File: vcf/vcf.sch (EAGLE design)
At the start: 102 parts, among them IC1 OPA4130U, IC2 OPA4130U, IC3 OPA4130U, IC4 OPA4130U, IC5 OPA4130U, Q1 BC847ASMD, Q2 BC847ASMD, Q3 BC847ASMD, Q4 BC847ASMD, Q5 BC847ASMD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

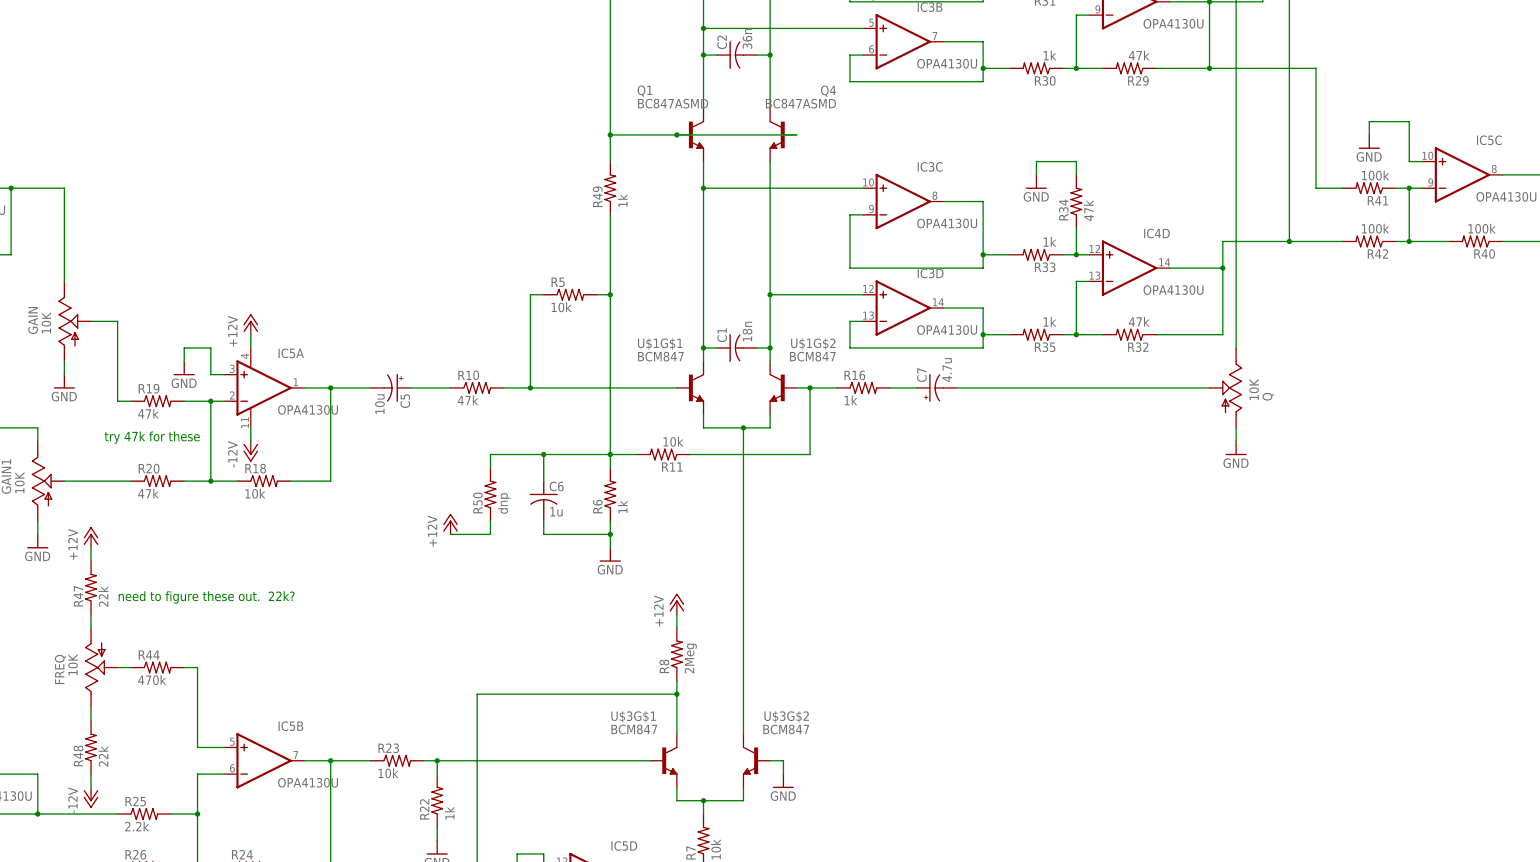
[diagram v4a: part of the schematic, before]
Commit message: fixed bugs in vca.  did more changing of vcf components.  need to route a trace in vcf
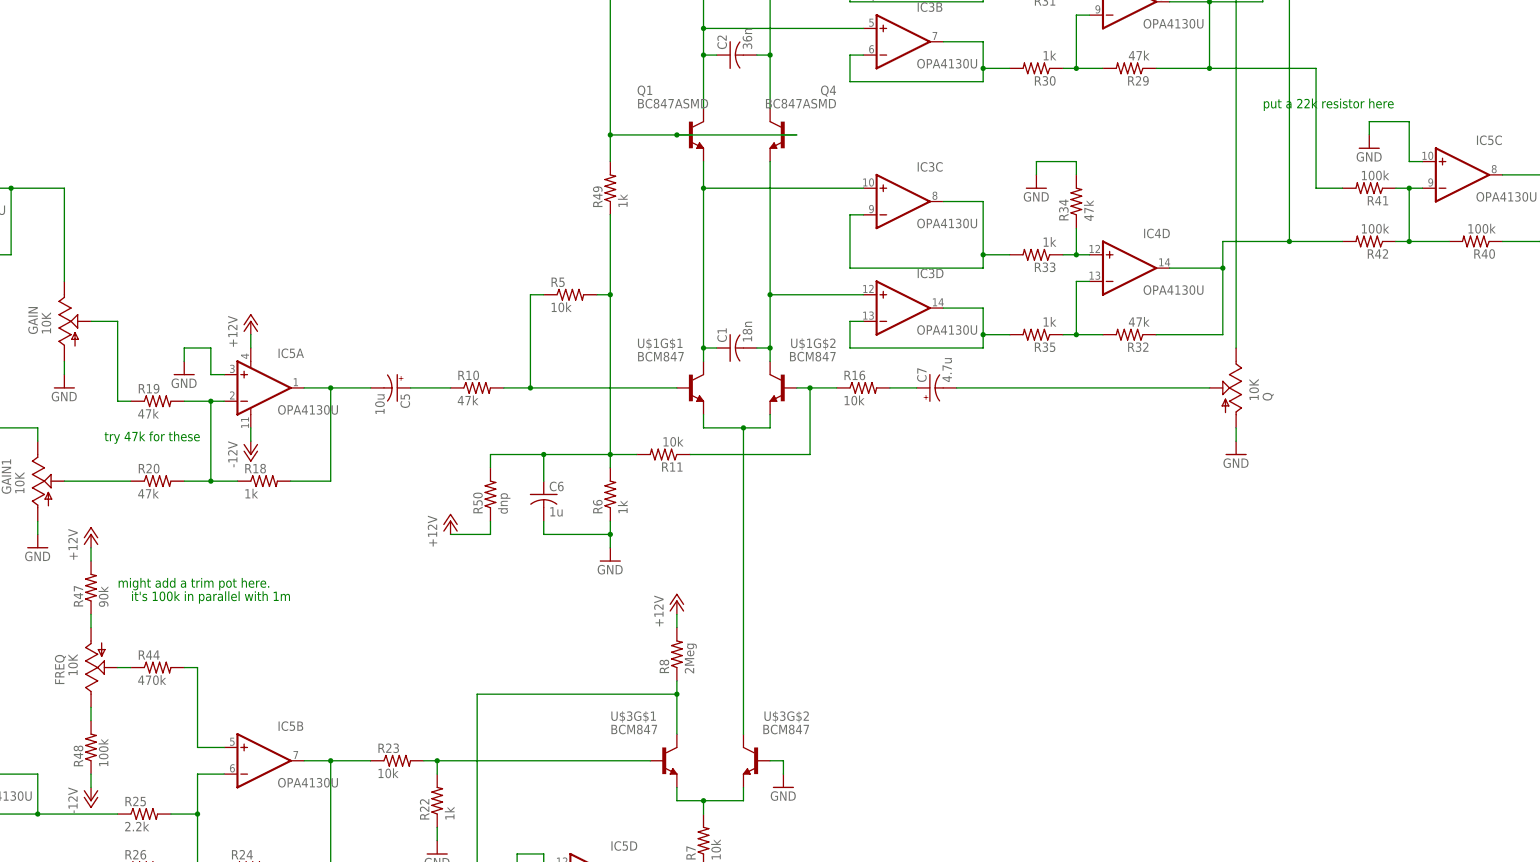
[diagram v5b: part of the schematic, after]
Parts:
- R16: value 1k -> 10k
- R18: value 10k -> 1k
- R47: value 22k -> 90k
- R48: value 22k -> 100k
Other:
- note added: "it's 100k in parallel with 1m"
- note added: "might add a trim pot here."
- note added: "put a 22k resistor here"
- note removed: "need to figure these out. 22k?"
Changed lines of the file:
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@@
 <part name="R15" library="dan" deviceset="R-US_" device="R0603" value="47k"/>
 <part name="GND5" library="dan" deviceset="GND" device=""/>
-<part name="R16" library="dan" deviceset="R-US_" device="R0603" value="1k"/>
+<part name="R16" library="dan" deviceset="R-US_" device="R0603" value="10k"/>
 <part name="Q" library="dan" deviceset="US-EVU" device="F2J" value="10K"/>
-<part name="R18" library="dan" deviceset="R-US_" device="R0603" value="10k"/>
+<part name="R18" library="dan" deviceset="R-US_" device="R0603" value="1k"/>
 <part name="R19" library="dan" deviceset="R-US_" device="R0603" value="47k"/>
 <part name="R20" library="dan" deviceset="R-US_" device="R0603" value="47k"/>
@@
 <part name="R45" library="dan" deviceset="R-US_" device="R0603" value="1k"/>
 <part name="R46" library="dan" deviceset="R-US_" device="R0603" value="1k"/>
-<part name="R47" library="dan" deviceset="R-US_" device="R0603" value="22k"/>
-<part name="R48" library="dan" deviceset="R-US_" device="R0603" value="22k"/>
+<part name="R47" library="dan" deviceset="R-US_" device="R0603" value="90k"/>
+<part name="R48" library="dan" deviceset="R-US_" device="R0603" value="100k"/>
 <part name="R49" library="dan" deviceset="R-US_" device="R0603" value="1k"/>
 <part name="P+11" library="dan" deviceset="+12V" device=""/>
@@
 <plain>
 <text x="-68.58" y="200.66" size="1.778" layer="91">Buffers have to be fet input.  Probably just make these TL084</text>
-<text x="-73.66" y="-2.54" size="1.778" layer="91">need to figure these out.  22k?</text>
+<text x="-73.66" y="0" size="1.778" layer="91">might add a trim pot here.</text>
 <text x="-76.2" y="27.94" size="1.778" layer="91">try 47k for these</text>
 <text x="104.14" y="185.42" size="1.778" layer="91">These gain resistors unverified</text>
 <text x="-68.58" y="198.12" size="1.778" layer="91">Make the instrumentation amps and summing amps opa4134</text>
+<text x="-71.12" y="-2.54" size="1.778" layer="91">it's 100k in parallel with 1m</text>
+<text x="144.78" y="91.44" size="1.778" layer="91">put a 22k resistor here</text>
 </plain>
 <instances>

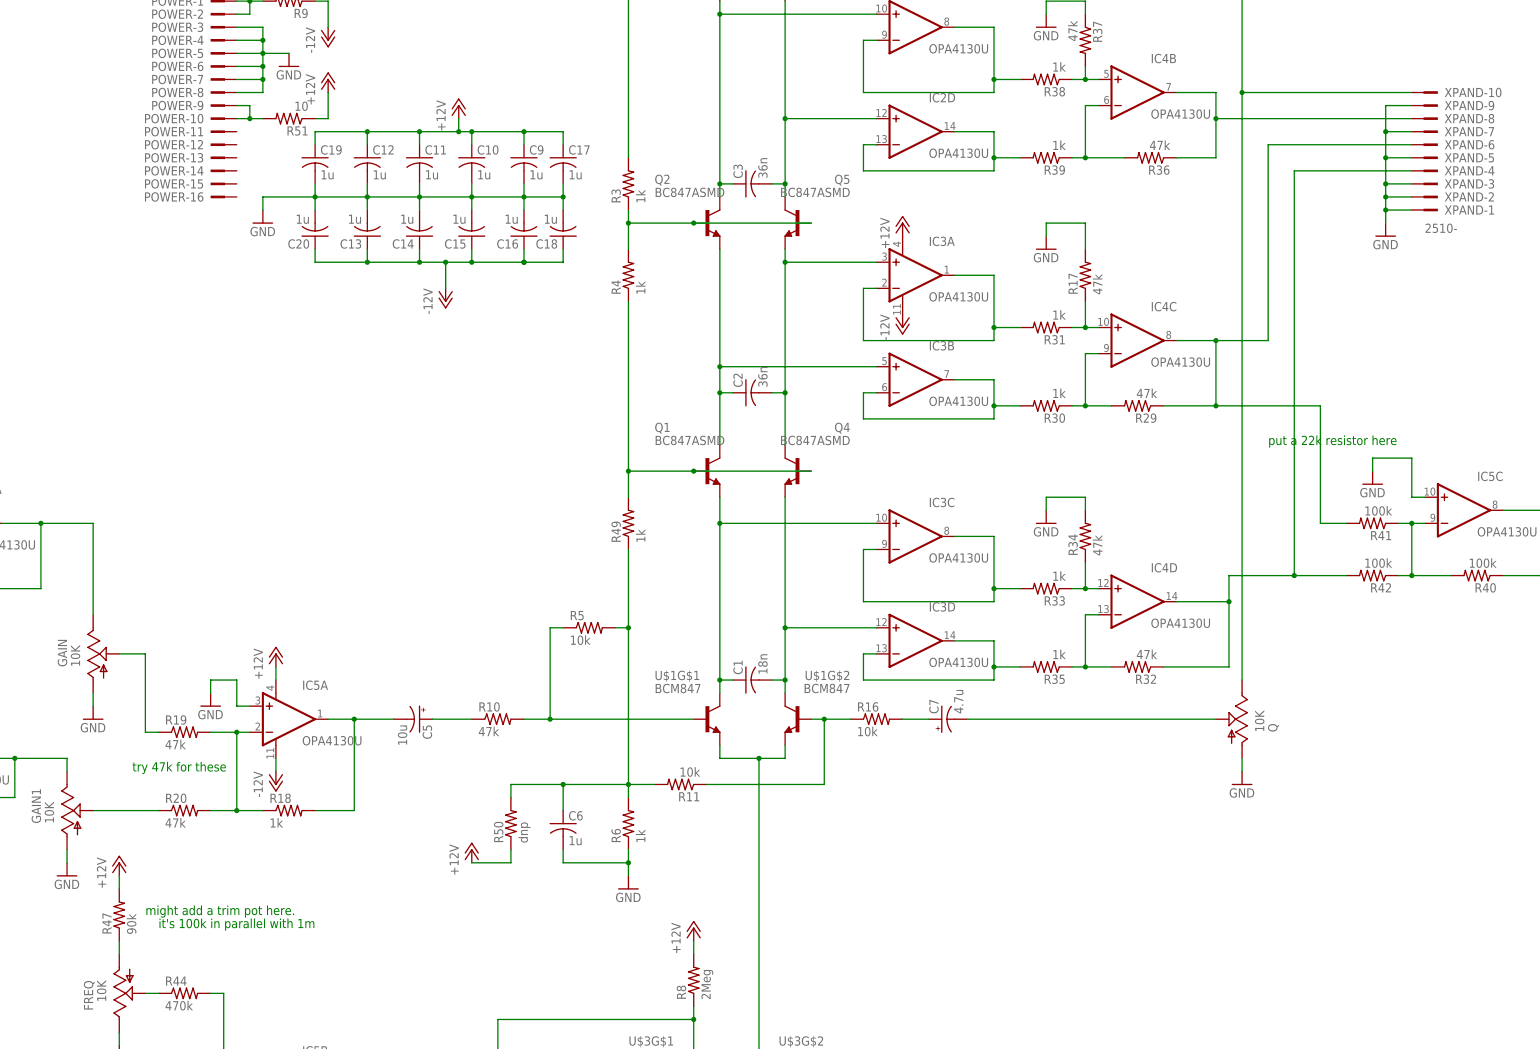
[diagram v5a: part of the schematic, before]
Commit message: made changes to vca after fab.  about ready to send 2nd rev of vcf in.
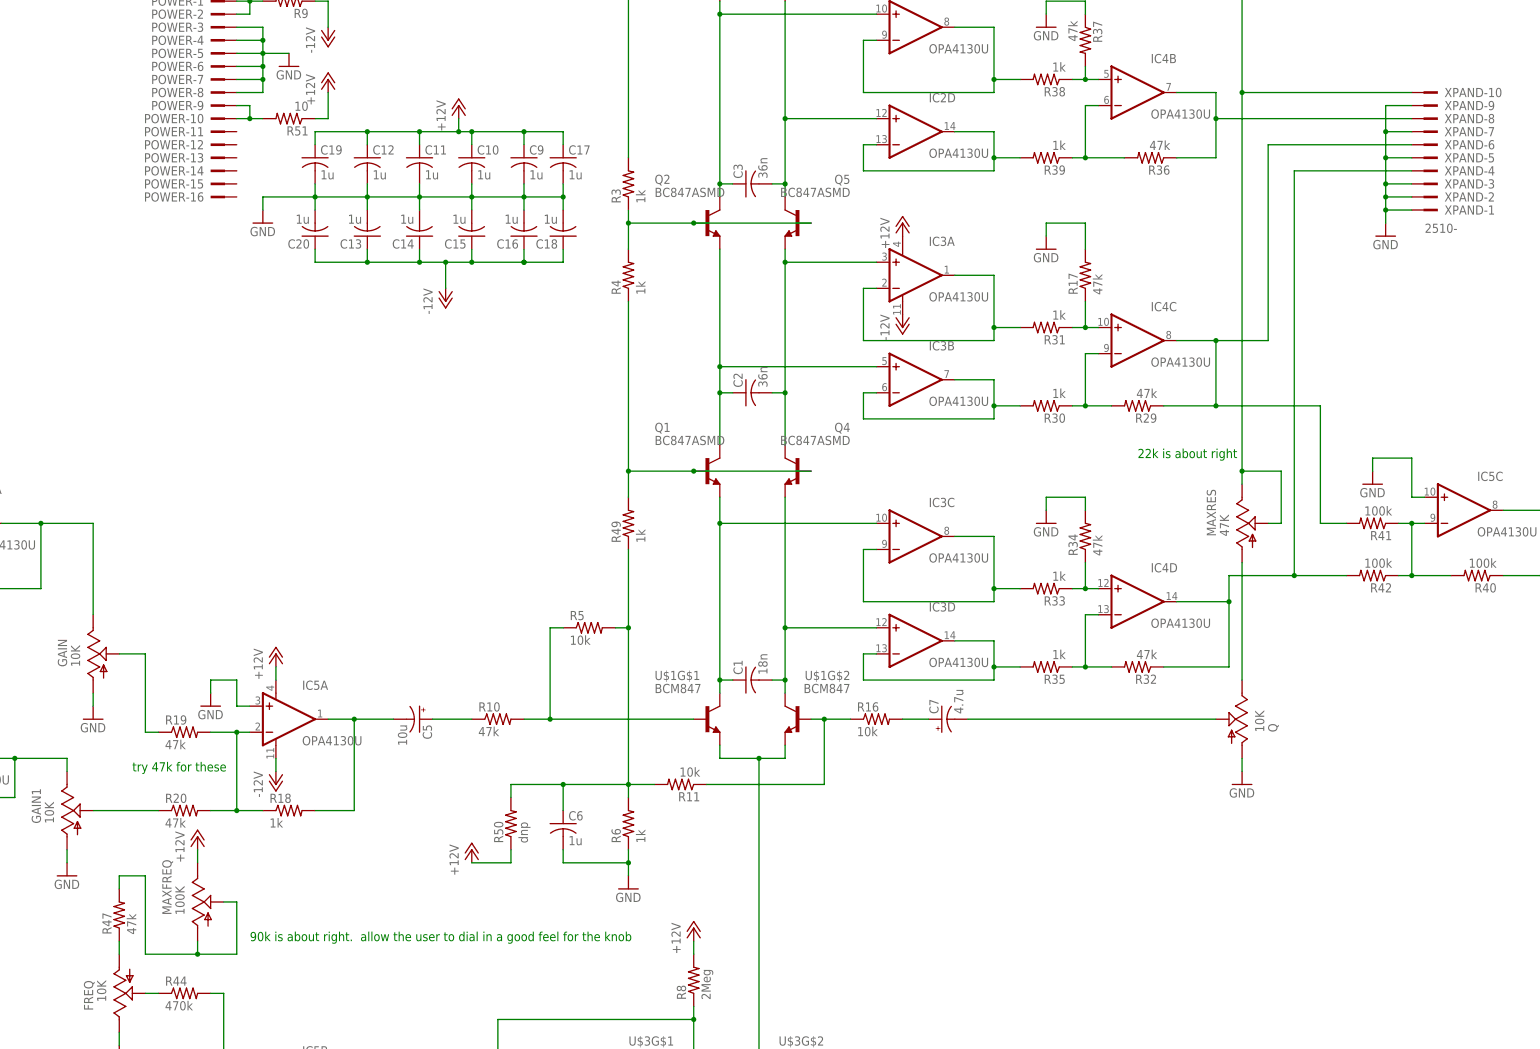
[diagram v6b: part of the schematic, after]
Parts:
- added MAXFREQ: 100K, dan:TRIM_US-S64W
- added MAXRES: 47K, dan:TRIM_US-S64W
- R47: value 90k -> 47k
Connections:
- new net N$73: MAXFREQ.A, MAXFREQ.S, R47.2
- new net N$74: MAXRES.A, Q.E
- net +12V: now also MAXFREQ.E; no longer R47.2
- net N$27: now also MAXRES.E, MAXRES.S; no longer Q.E
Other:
- note added: "22k is about right"
- note added: "90k is about right. allow the user to dial in a good feel for the knob"
- note removed: "it's 100k in parallel with 1m"
- note removed: "might add a trim pot here."
- note removed: "put a 22k resistor here"
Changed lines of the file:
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@@
 <part name="R45" library="dan" deviceset="R-US_" device="R0603" value="1k"/>
 <part name="R46" library="dan" deviceset="R-US_" device="R0603" value="1k"/>
-<part name="R47" library="dan" deviceset="R-US_" device="R0603" value="90k"/>
+<part name="R47" library="dan" deviceset="R-US_" device="R0603" value="47k"/>
 <part name="R48" library="dan" deviceset="R-US_" device="R0603" value="100k"/>
 <part name="R49" library="dan" deviceset="R-US_" device="R0603" value="1k"/>
@@
 <part name="R9" library="dan" deviceset="R-US_" device="R0603" value="10"/>
 <part name="R51" library="dan" deviceset="R-US_" device="R0603" value="10"/>
+<part name="MAXFREQ" library="dan" deviceset="TRIM_US-" device="S64W" value="100K"/>
+<part name="MAXRES" library="dan" deviceset="TRIM_US-" device="S64W" value="47K"/>
 </parts>
 <sheets>
@@
 <plain>
 <text x="-68.58" y="200.66" size="1.778" layer="91">Buffers have to be fet input.  Probably just make these TL084</text>
-<text x="-73.66" y="0" size="1.778" layer="91">might add a trim pot here.</text>
 <text x="-76.2" y="27.94" size="1.778" layer="91">try 47k for these</text>
 <text x="104.14" y="185.42" size="1.778" layer="91">These gain resistors unverified</text>
 <text x="-68.58" y="198.12" size="1.778" layer="91">Make the instrumentation amps and summing amps opa4134</text>
-<text x="-71.12" y="-2.54" size="1.778" layer="91">it's 100k in parallel with 1m</text>
-<text x="144.78" y="91.44" size="1.778" layer="91">put a 22k resistor here</text>
+<text x="119.38" y="88.9" size="1.778" layer="91">22k is about right</text>
+<text x="-53.34" y="-5.08" size="1.778" layer="91">90k is about right.  allow the user to dial in a good feel for the knob</text>
 </plain>
 <instances>
@@
 <instance part="FREQ" gate="G$1" x="-78.74" y="-15.24" rot="MR180"/>
 <instance part="P-7" gate="1" x="-78.74" y="-40.64"/>
-<instance part="P+9" gate="1" x="-78.74" y="10.16"/>
+<instance part="P+9" gate="1" x="-63.5" y="15.24"/>
 <instance part="R44" gate="G$1" x="-66.04" y="-15.24"/>
 <instance part="GAIN1" gate="G$1" x="-88.9" y="20.32"/>
@@
 <instance part="R9" gate="G$1" x="-45.72" y="177.8" rot="R180"/>
 <instance part="R51" gate="G$1" x="-45.72" y="154.94" rot="R180"/>
+<instance part="MAXFREQ" gate="G$1" x="-63.5" y="2.54"/>
+<instance part="MAXRES" gate="G$1" x="139.7" y="76.2"/>
 </instances>
 <busses>
@@
 </segment>
 <segment>
-<pinref part="R47" gate="G$1" pin="2"/>
-<pinref part="P+9" gate="1" pin="+12V"/>
-<wire x1="-78.74" y1="7.62" x2="-78.74" y2="5.08" width="0.1524" layer="91"/>
-</segment>
-<segment>
 <pinref part="P+11" gate="1" pin="+12V"/>
 <wire x1="-10.16" y1="10.16" x2="-2.54" y2="10.16" width="0.1524" layer="91"/>
@@
 <pinref part="P+12" gate="1" pin="+12V"/>
 <wire x1="-134.62" y1="-2.54" x2="-134.62" y2="2.54" width="0.1524" layer="91"/>
+</segment>
+<segment>
+<pinref part="MAXFREQ" gate="G$1" pin="E"/>
+<pinref part="P+9" gate="1" pin="+12V"/>
+<wire x1="-63.5" y1="12.7" x2="-63.5" y2="10.16" width="0.1524" layer="91"/>
 </segment>
 </net>
@@
 <wire x1="139.7" y1="203.2" x2="127" y2="203.2" width="0.1524" layer="91"/>
 <pinref part="IC4" gate="A" pin="OUT"/>
-<pinref part="Q" gate="G$1" pin="E"/>
-<wire x1="139.7" y1="45.72" x2="139.7" y2="160.02" width="0.1524" layer="91"/>
-<junction x="139.7" y="160.02"/>
 <pinref part="C21" gate="G$1" pin="-"/>
 <wire x1="149.86" y1="193.04" x2="139.7" y2="193.04" width="0.1524" layer="91"/>
 <junction x="139.7" y="193.04"/>
+<pinref part="MAXRES" gate="G$1" pin="E"/>
+<wire x1="139.7" y1="160.02" x2="139.7" y2="86.36" width="0.1524" layer="91"/>
+<junction x="139.7" y="160.02"/>
+<pinref part="MAXRES" gate="G$1" pin="S"/>
+<wire x1="139.7" y1="86.36" x2="139.7" y2="83.82" width="0.1524" layer="91"/>
+<wire x1="144.78" y1="76.2" x2="147.32" y2="76.2" width="0.1524" layer="91"/>
+<wire x1="147.32" y1="76.2" x2="147.32" y2="86.36" width="0.1524" layer="91"/>
+<wire x1="147.32" y1="86.36" x2="139.7" y2="86.36" width="0.1524" layer="91"/>
+<junction x="139.7" y="86.36"/>
 </segment>
 </net>
@@
 </segment>
 </net>
+<net name="N$73" class="0">
+<segment>
+<wire x1="-55.88" y1="2.54" x2="-55.88" y2="-7.62" width="0.1524" layer="91"/>
+<wire x1="-55.88" y1="-7.62" x2="-63.5" y2="-7.62" width="0.1524" layer="91"/>
+<pinref part="MAXFREQ" gate="G$1" pin="A"/>
+<wire x1="-63.5" y1="-7.62" x2="-63.5" y2="-5.08" width="0.1524" layer="91"/>
+<wire x1="-63.5" y1="-7.62" x2="-73.66" y2="-7.62" width="0.1524" layer="91"/>
+<wire x1="-73.66" y1="-7.62" x2="-73.66" y2="7.62" width="0.1524" layer="91"/>
+<pinref part="R47" gate="G$1" pin="2"/>
+<wire x1="-73.66" y1="7.62" x2="-78.74" y2="7.62" width="0.1524" layer="91"/>
+<wire x1="-78.74" y1="7.62" x2="-78.74" y2="5.08" width="0.1524" layer="91"/>
+<junction x="-63.5" y="-7.62"/>
+<pinref part="MAXFREQ" gate="G$1" pin="S"/>
+<wire x1="-58.42" y1="2.54" x2="-55.88" y2="2.54" width="0.1524" layer="91"/>
+</segment>
+</net>
+<net name="N$74" class="0">
+<segment>
+<pinref part="MAXRES" gate="G$1" pin="A"/>
+<pinref part="Q" gate="G$1" pin="E"/>
+<wire x1="139.7" y1="68.58" x2="139.7" y2="45.72" width="0.1524" layer="91"/>
+</segment>
+</net>
